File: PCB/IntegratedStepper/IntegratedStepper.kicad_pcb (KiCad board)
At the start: 4 copper layers, 42 x 42.5 mm, 75 parts, among them IC2 SN65HVD230DR, IC3 LMR38020FSQDDARQ1, J3 Screw_Terminal_01x02, J4 Screw_Terminal_01x02, J5 Conn_01x05_Socket, Q1 SS8050-G, Q2 SS8050-G, U1 ESP32-WROOM-32E, U2 AS5048A, U3 CP2102N-Axx-xQFN28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

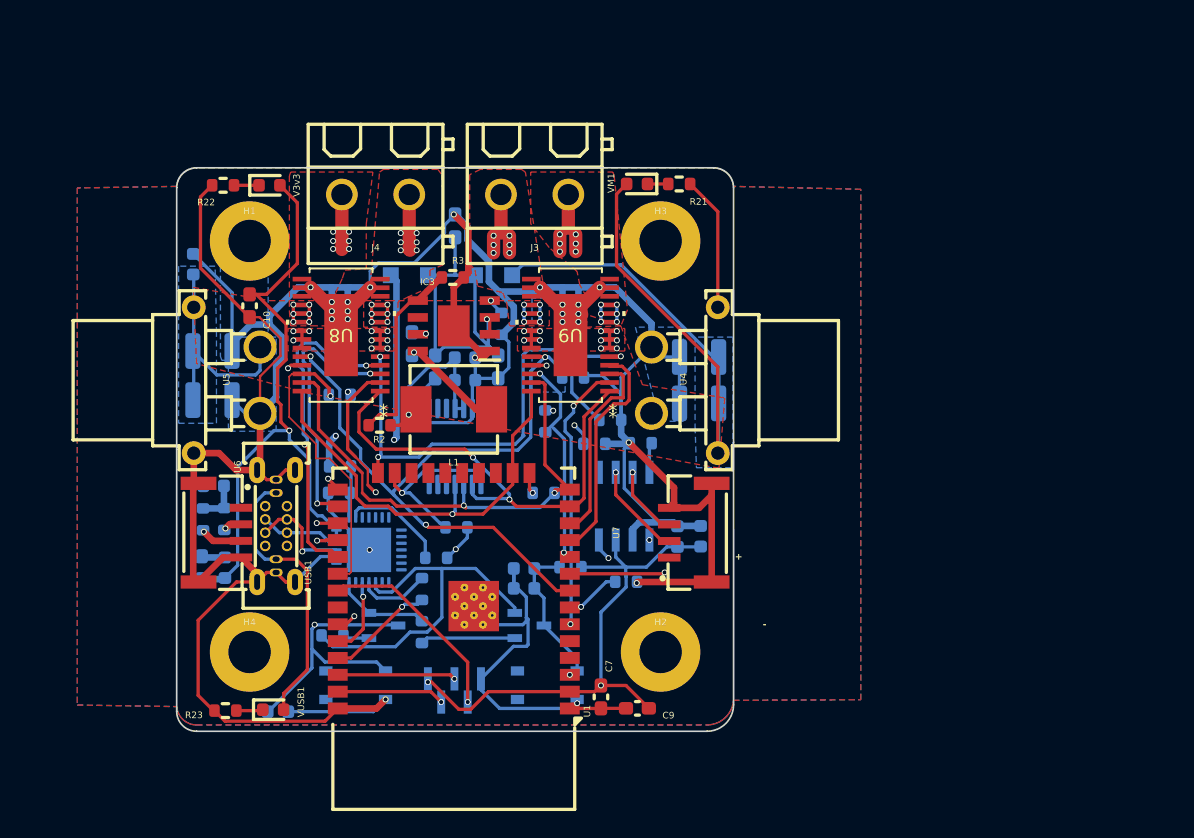
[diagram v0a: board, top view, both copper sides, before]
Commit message: update layout for larger pcb
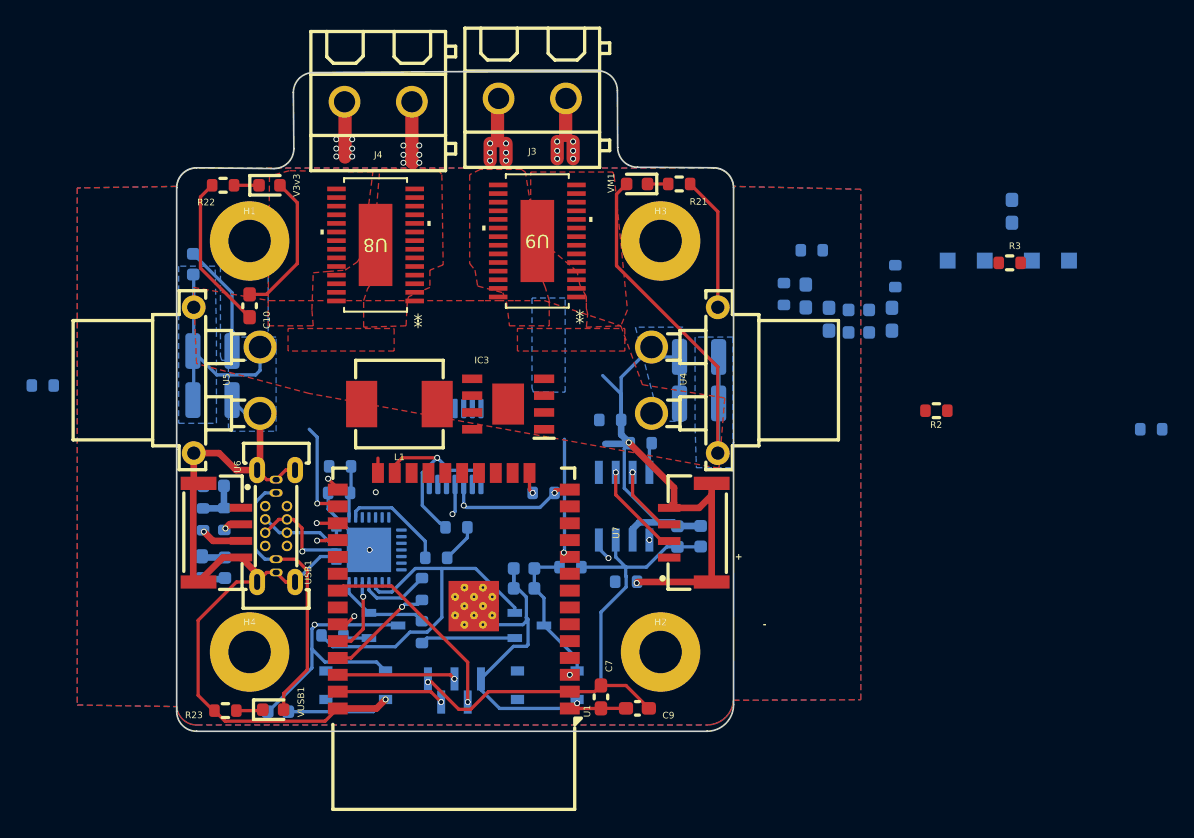
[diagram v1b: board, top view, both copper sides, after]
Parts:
- moved D2 42.0 mm to (159.6, 107.0)
- moved R2 42.0 mm to (157.3, 118.3)
- moved C6 42.0 mm to (163.0, 103.3)
- moved D1 42.0 mm to (165.9, 107.0)
- moved R_IPROP1 42.0 mm to (173.5, 119.7)
- moved R3 42.0 mm to (162.8, 107.2)
- moved C11 29.9 mm to (147.4, 109.7)
- moved C16 29.9 mm to (151.4, 110.7)
- moved C17 29.9 mm to (151.4, 112.4)
- moved C4 29.9 mm to (149.2, 111.4)
- moved C5 29.9 mm to (153.9, 111.4)
- moved R4 29.9 mm to (154.2, 108.2)
- moved R_nFAULT_2 22.4 mm to (89.9, 116.4)
- moved R_nFAULT_1 20.4 mm to (145.8, 109.5)
- moved R_nSLEEP1 20.4 mm to (147.9, 106.2)
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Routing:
- net GND: track 372.4 -> 242.3 mm, vias 24 -> 6
- net 3V3_VCC: track 176.6 -> 57.1 mm, vias 7 -> 1
- net IPROPI_2: track 53.8 -> 0.00 mm, vias 2 -> 0
- net /DRV8245/NSLEEP: track 51.4 -> 0.00 mm, vias 3 -> 0
- net /DRV8245/DRVOFF: track 40.1 -> 1.12 mm, vias 3 -> 0
- net /DRV8245/M_SCLK: track 36.1 -> 0.00 mm, vias 2 -> 0
- net IPROPI_1: track 32.9 -> 0.00 mm, vias 3 -> 0
- net /DRV8245/M_MOSI: track 32.9 -> 2.32 mm
- net VIN: track 29.1 -> 0.00 mm, vias 1 -> 0
- net /DRV8245/M_MISO: track 39.9 -> 11.1 mm
- net /3V3_VReg/V_USB: track 48.2 -> 21.4 mm, vias 2 -> 0
- net IN3: track 24.9 -> 0.00 mm, vias 2 -> 0
- net /3V3_VReg/VM: track 119.8 -> 96.2 mm, vias 19 -> 0
- net /DRV8245/NFAULT_2: track 22.4 -> 0.00 mm, vias 1 -> 0
- net /DRV8245/DRV1_CS: track 20.4 -> 0.00 mm, vias 2 -> 0
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- removed copper zone on In2.Cu, net GND
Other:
- board size 42 x 42.5 mm -> 42 x 49.8 mm

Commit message: Update semi-final layout for HVSSOP DRV8245
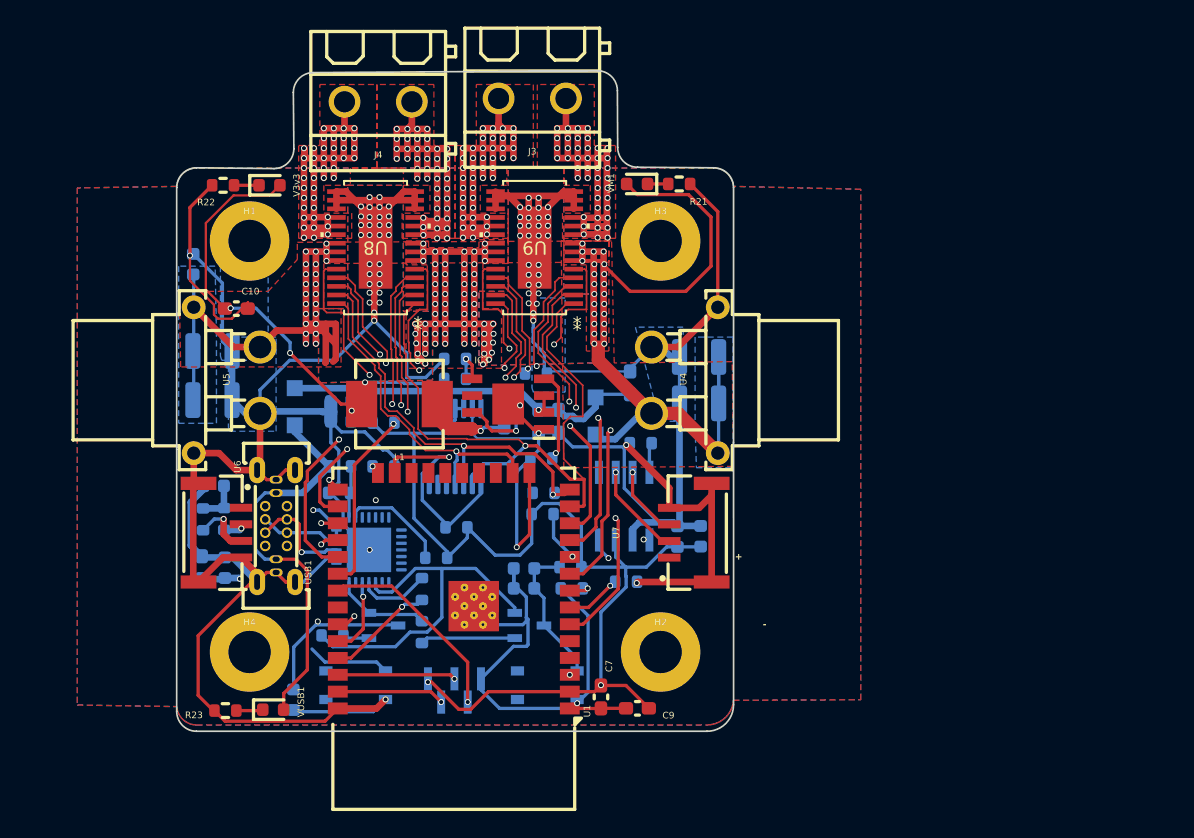
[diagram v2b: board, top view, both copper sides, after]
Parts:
- R2, R3: moved to B.Cu
- moved D2 51.8 mm to (108.9, 118.0), turned to -90 degrees
- moved R_IPROP1 46.6 mm to (127.1, 115.5)
- moved R3 42.4 mm to (121.0, 114.4), turned to 180 degrees
- moved C16 39.7 mm to (112.4, 117.6), turned to 180 degrees
- moved C17 39.6 mm to (112.4, 119.1), turned to 180 degrees
- moved R2 36.4 mm to (121.0, 115.9), turned to 0 degrees
- moved D1 36.2 mm to (131.6, 118.7), turned to -90 degrees
- moved C6 31.6 mm to (134.2, 116.2)
- moved R_nSLEEP1 31.3 mm to (129.8, 131.7), turned to 0 degrees
- moved R4 30.0 mm to (127.5, 121.9), turned to 180 degrees
- moved C5 26.3 mm to (128.8, 119.1)
- moved R_nFAULT_2 25.9 mm to (115.6, 119.2), turned to 180 degrees
- moved R_nFAULT_1 24.6 mm to (127.6, 126.1), turned to 180 degrees
- moved C11 24.5 mm to (124.7, 118.7)
- moved C4 23.2 mm to (127.3, 119.1)
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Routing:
- net GND: track 242.3 -> 378.1 mm, vias 6 -> 69
- net /3V3_VReg/VM: track 96.2 -> 215.6 mm, vias 0 -> 112
- net 3V3_VCC: track 57.1 -> 142.8 mm, vias 1 -> 8
- net /DRV8245/NSLEEP: track 0.00 -> 71.8 mm, vias 0 -> 3
- net IPROPI_2: track 0.00 -> 67.7 mm, vias 0 -> 2
- net /DRV8245/M_SCLK: track 0.00 -> 50.6 mm, vias 0 -> 1
- net /DRV8245/DRVOFF: track 1.12 -> 38.8 mm, vias 0 -> 3
- net /DRV8245/M_MOSI: track 2.32 -> 38.8 mm, vias 1 -> 2
- net /DRV8245/M_MISO: track 11.1 -> 45.9 mm, vias 2 -> 3
- net IPROPI_1: track 0.00 -> 31.3 mm, vias 0 -> 2
- net /DRV8245/DRV1_CS: track 0.00 -> 30.8 mm, vias 0 -> 2
- net VIN: track 0.00 -> 28.8 mm, vias 0 -> 1
- net /DRV8245/NFAULT_2: track 0.00 -> 28.5 mm, vias 0 -> 2
- net IN3: track 0.00 -> 27.7 mm, vias 0 -> 2
- net IN1: track 0.00 -> 25.7 mm, vias 0 -> 2
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- added copper zone on In2.Cu, net GND
- removed copper zone on In2.Cu, net /3V3_VReg/VM

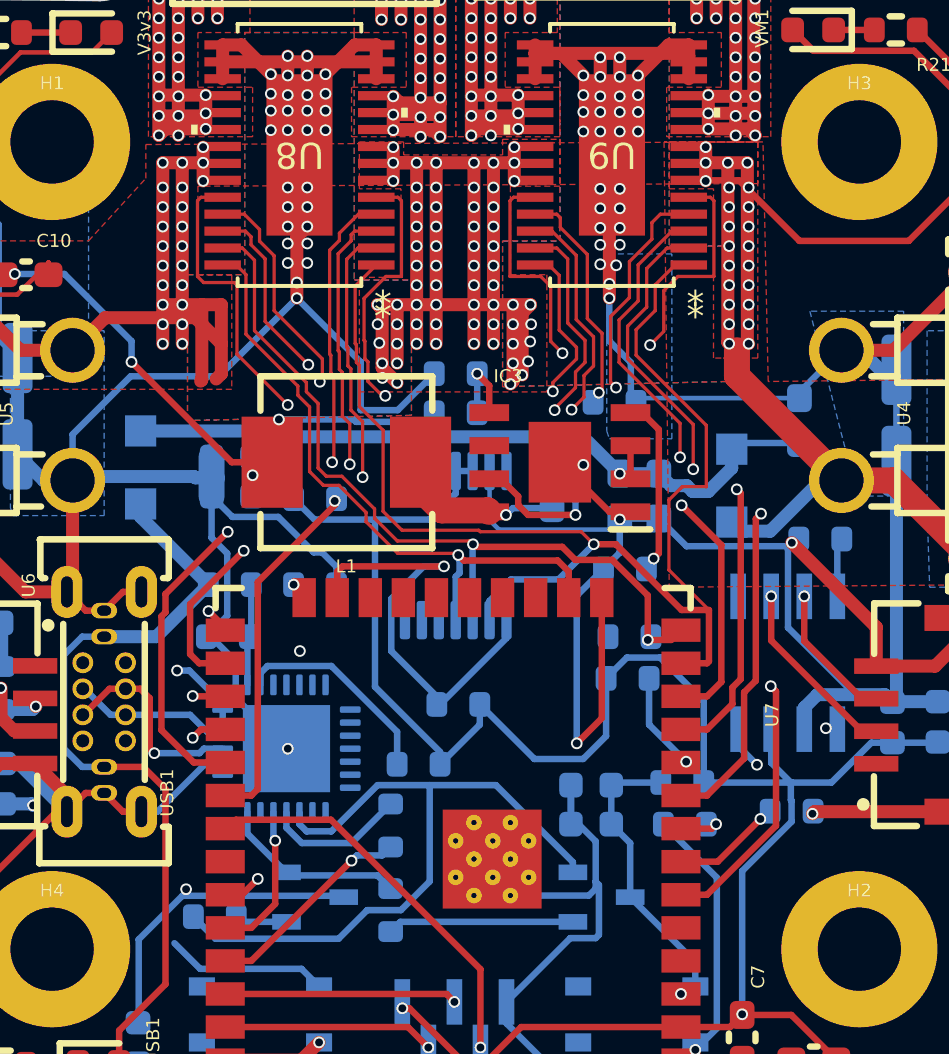
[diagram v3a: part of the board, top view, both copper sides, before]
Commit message: updated CS to be on IO instead of just input pin
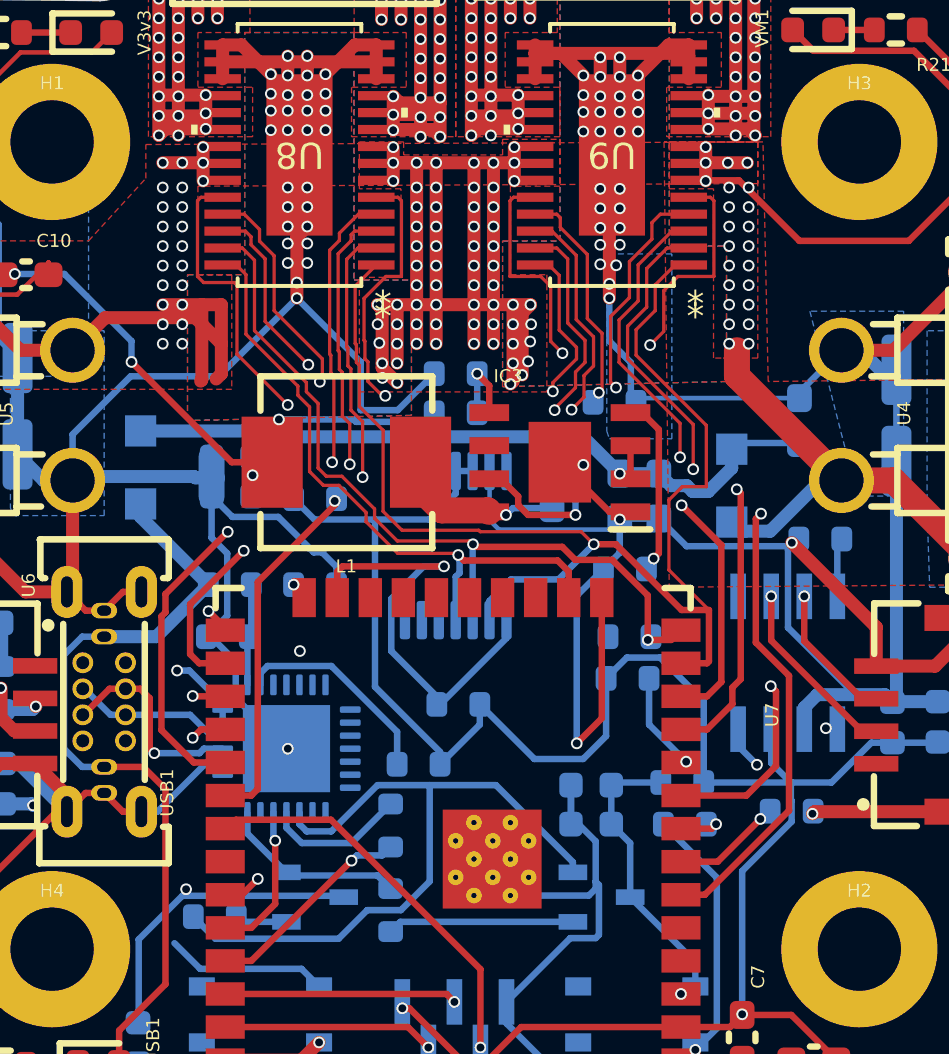
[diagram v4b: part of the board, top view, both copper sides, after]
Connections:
- U1 pad 6: /DRV8245/DRV1_CS -> IPROPI_1
- U1 pad 9: IPROPI_1 -> /DRV8245/DRV1_CS
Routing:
- net IPROPI_1: track 31.3 -> 36.1 mm
- net /DRV8245/DRV1_CS: track 30.8 -> 27.8 mm
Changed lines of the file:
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@@
 			(size 1.5 0.9)
 			(layers "F.Cu" "F.Paste" "F.Mask")
-			(net 45 "/DRV8245/DRV1_CS")
+			(net 17 "IPROPI_1")
 			(pinfunction "IO34")
 			(pintype "input")
@@
 			(size 1.5 0.9)
 			(layers "F.Cu" "F.Paste" "F.Mask")
-			(net 17 "IPROPI_1")
+			(net 45 "/DRV8245/DRV1_CS")
 			(pinfunction "IO33")
 			(pintype "bidirectional")
@@
 				(font
 					(size 1.27 1.27)
-					(thickness 0.15)
 				)
 				(justify mirror)
@@
 				(font
 					(size 1.27 1.27)
-					(thickness 0.15)
 				)
 				(justify mirror)
@@
 				(font
 					(size 1.27 1.27)
-					(thickness 0.15)
 				)
 				(justify mirror)
@@
 				(font
 					(size 1.27 1.27)
-					(thickness 0.15)
 				)
 				(justify mirror)
@@
 				(font
 					(size 1.27 1.27)
-					(thickness 0.15)
 				)
 				(justify mirror)
@@
 				(font
 					(size 1.27 1.27)
-					(thickness 0.15)
 				)
 				(justify mirror)
@@
 	)
 	(segment
-		(start 110.5 106.3)
-		(end 110.5 113.25)
-		(width 0.5)
-		(layer "F.Cu")
-		(net 1)
-	)
-	(segment
 		(start 135.8125 118.5)
 		(end 137.8125 118.5)
@@
 	)
 	(segment
-		(start 109.75 106.3)
-		(end 109.75 113.25)
-		(width 0.5)
-		(layer "F.Cu")
-		(net 1)
-	)
-	(segment
 		(start 118.75 111.75)
 		(end 118.75 114)
@@
 	)
 	(segment
-		(start 132.2 113.2)
-		(end 132.25 113.25)
-		(width 0.5)
-		(layer "F.Cu")
-		(net 1)
-	)
-	(segment
 		(start 132.2 106.3)
 		(end 130.6 106.3)
@@
 	)
 	(segment
-		(start 132.2 106.3)
-		(end 132.2 113.2)
-		(width 0.5)
-		(layer "F.Cu")
-		(net 1)
-	)
-	(segment
 		(start 107.537499 112.250001)
 		(end 111.000001 112.250001)
@@
 	)
 	(segment
-		(start 131.45 106.3)
-		(end 131.45 113.2)
-		(width 0.5)
-		(layer "F.Cu")
-		(net 1)
-	)
-	(segment
-		(start 131.45 113.2)
-		(end 131.5 113.25)
-		(width 0.5)
-		(layer "F.Cu")
-		(net 1)
-	)
-	(segment
 		(start 123.2 111.75)
 		(end 123.2 114.7)
@@
 	)
 	(segment
+		(start 131.45 106.3)
+		(end 131.45 113.2)
+		(width 1)
+		(layer "In2.Cu")
+		(net 1)
+	)
+	(segment
 		(start 111.3 106.3)
 		(end 132.2 106.3)
@@
 	)
 	(segment
+		(start 132.25 106.35)
+		(end 132.2 106.3)
+		(width 1)
+		(layer "In2.Cu")
+		(net 1)
+	)
+	(segment
+		(start 109.75 113.25)
+		(end 109.75 106.3)
+		(width 1)
+		(layer "In2.Cu")
+		(net 1)
+	)
+	(segment
+		(start 110.5 106.3)
+		(end 110.5 113.25)
+		(width 1)
+		(layer "In2.Cu")
+		(net 1)
+	)
+	(segment
+		(start 131.45 113.2)
+		(end 131.5 113.25)
+		(width 1)
+		(layer "In2.Cu")
+		(net 1)
+	)
+	(segment
+		(start 132.25 113.25)
+		(end 132.25 106.35)
+		(width 1)
+		(layer "In2.Cu")
+		(net 1)
+	)
+	(segment
 		(start 107.5 113.5)
 		(end 105.5 113.5)
@@
 	)
 	(segment
-		(start 132.524265 119.975649)
-		(end 132.725692 119.774222)
+		(start 133.8 126)
+		(end 133.8 131.177818)
 		(width 0.25)
 		(layer "F.Cu")
@@
 	)
 	(segment
-		(start 132.075 129.175)
-		(end 132.075 126.637792)
-		(width 0.25)
+		(start 124.879101 108.274999)
+		(end 125.015601 108.411499)
+		(width 0.127)
 		(layer "F.Cu")
 		(net 17)
 	)
 	(segment
-		(start 132.075 126.637792)
-		(end 132.524265 126.188527)
+		(start 130.567818 134.41)
+		(end 129.65 134.41)
 		(width 0.25)
 		(layer "F.Cu")
@@
 	)
 	(segment
-		(start 124.879101 108.274999)
-		(end 125.015601 108.411499)
-		(width 0.127)
-		(layer "F.Cu")
-		(net 17)
-	)
-	(segment
-		(start 130.65 130.6)
-		(end 132.075 129.175)
+		(start 132.524265 119.975649)
+		(end 132.725692 119.774222)
 		(width 0.25)
 		(layer "F.Cu")
@@
 	)
 	(segment
-		(start 132.524265 126.188527)
-		(end 132.524265 119.975649)
+		(start 133.8 131.177818)
+		(end 130.567818 134.41)
 		(width 0.25)
 		(layer "F.Cu")
@@
 	)
 	(segment
+		(start 132.524265 124.724265)
+		(end 132.524265 119.975649)
+		(width 0.25)
+		(layer "F.Cu")
+		(net 17)
+	)
+	(segment
 		(start 126.054 112.283619)
 		(end 126.6195 112.849119)
@@
 	)
 	(segment
+		(start 133.8 126)
+		(end 132.524265 124.724265)
+		(width 0.25)
+		(layer "F.Cu")
+		(net 17)
+	)
+	(segment
 		(start 125.015601 108.411499)
 		(end 125.015601 108.782277)
@@
 		(net 17)
 	)
-	(segment
-		(start 129.65 130.6)
-		(end 130.65 130.6)
-		(width 0.25)
-		(layer "F.Cu")
-		(net 17)
-	)
 	(via
 		(at 132.725692 119.774222)
@@
 	)
 	(segment
+		(start 132.163762 130.6)
+		(end 133.3 129.463762)
+		(width 0.25)
+		(layer "F.Cu")
+		(net 45)
+	)
+	(segment
 		(start 128.3345 110.361398)
 		(end 128.3345 111.841497)
@@
 	)
 	(segment
-		(start 130.65 134.41)
-		(end 133.3 131.76)
-		(width 0.25)
-		(layer "F.Cu")
-		(net 45)
-	)
-	(segment
-		(start 133.3 126.6)
-		(end 133.1 126.4)
-		(width 0.25)
-		(layer "F.Cu")
-		(net 45)
-	)
-	(segment
 		(start 129.120899 109.574999)
 		(end 128.3345 110.361398)
@@
 	)
 	(segment
-		(start 129.65 134.41)
-		(end 130.65 134.41)
-		(width 0.25)
+		(start 128.3345 111.841497)
+		(end 127.6005 112.575497)
+		(width 0.127)
 		(layer "F.Cu")
 		(net 45)
 	)
 	(segment
-		(start 128.3345 111.841497)
-		(end 127.6005 112.575497)
-		(width 0.127)
+		(start 133.3 126.6)
+		(end 133.1 126.4)
+		(width 0.25)
 		(layer "F.Cu")
 		(net 45)
 	)
 	(segment
-		(start 133.3 131.76)
+		(start 133.3 129.463762)
 		(end 133.3 126.6)
 		(width 0.25)
@@
 		(layer "F.Cu")
 		(net 45)
+	)
+	(segment
+		(start 129.65 130.6)
+		(end 132.163762 130.6)
+		(width 0.25)
+		(layer "F.Cu")
+		(net 45)
